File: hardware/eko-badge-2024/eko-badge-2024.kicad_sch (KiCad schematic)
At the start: 51 parts, among them J1 UART, J2 Battery, J3 Lentes, J4 OLED, J7 Battery, P1 USB_C_Plug_USB2.0, Q1 DMG3415U-7, SW1 ON, SW2 LEFT, SW3 UP, SW4 DOWN, SW5 RESET, SW6 BOOT, SW7 RIGTH, U1 ESP32-C6-WROOM-1-N4, U2 AP2112K-3.3, U3 RFM95W-868S2, U4 TPA321

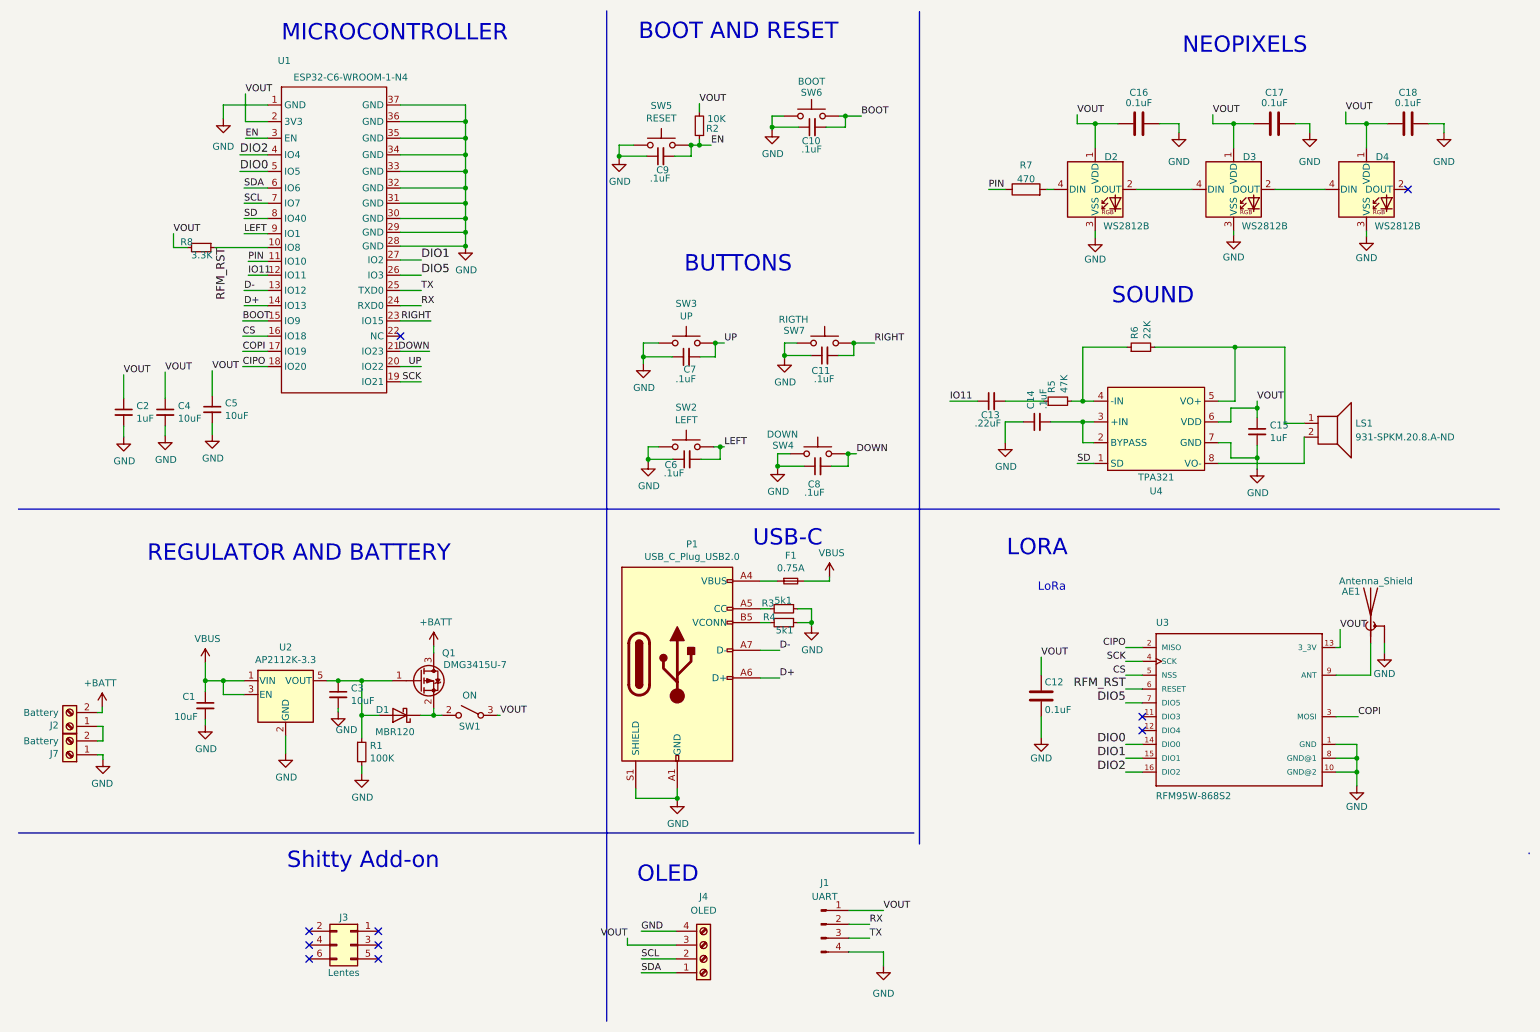
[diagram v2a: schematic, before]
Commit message: feat(Hw):Update_Layer_Distribution
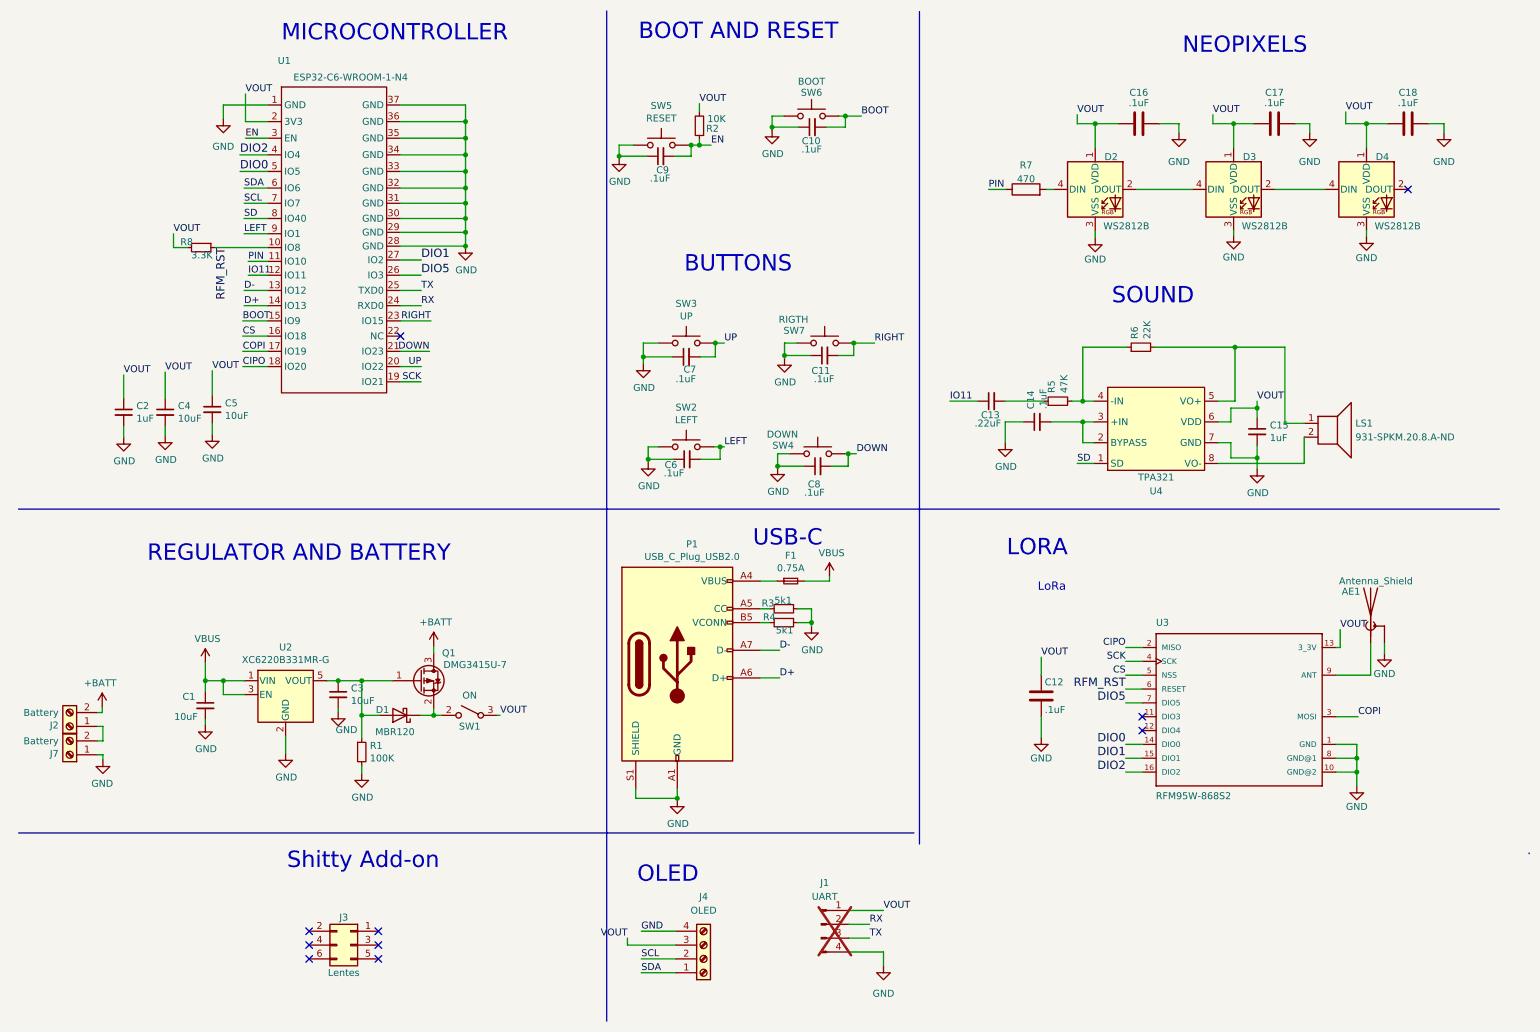
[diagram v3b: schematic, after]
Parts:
- C10, C11, C14, C6, C7, C8, C9: Proveedor (none) -> LCSC; manf# (none) -> 0603F104M500NT
- C12: value 0.1uF -> .1uF; LCSC# C42998 -> C478888; Proveedor (none) -> LCSC
- C13: LCSC# C478888 -> C161213; Proveedor (none) -> LCSC
- C15: Proveedor (none) -> JLCPCB; manf# (none) -> TMK107BJ105KA8T
- C16, C17, C18: value 0.1uF -> .1uF; LCSC# C42998 -> C478888
- J1: now not fitted
- P1: LCSC# C2987386 -> C393939; Proveedor (none) -> LCSC
- SW2, SW3, SW4, SW5, SW6, SW7: Proveedor (none) -> LCSC
- U2: value AP2112K-3.3 -> XC6220B331MR-G; LCSC# C51118 -> C86534; manf# AP2112K3.3TRG -> XC6220B331MR-G
- U3: Proveedor (none) -> Mouser
- U4: LCSC# C329448 -> C2873032; Proveedor (none) -> LCSC
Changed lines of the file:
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@@
 			)
 		)
-		(property "manf#" ""
+		(property "manf#" "0603F104M500NT"
 			(at 198.374 88.138 0)
 			(effects
@@
 			)
 		)
+		(property "Proveedor" "LCSC"
+			(at 198.374 88.138 0)
+			(effects
+				(font
+					(size 1.27 1.27)
+				)
+				(hide yes)
+			)
+		)
 		(pin "1"
 		)
@@
 			)
 		)
-		(property "LCSC#" "C329448"
+		(property "LCSC#" "C2873032"
+			(at 220.218 93.218 0)
+			(effects
+				(font
+					(size 1.27 1.27)
+				)
+				(hide yes)
+			)
+		)
+		(property "Proveedor" "LCSC"
 			(at 220.218 93.218 0)
 			(effects
@@
 			)
 		)
-		(property "manf#" ""
+		(property "manf#" "0603F104M500NT"
 			(at 129.286 39.37 0)
 			(effects
@@
 			)
 		)
+		(property "Proveedor" "LCSC"
+			(at 129.286 39.37 0)
+			(effects
+				(font
+					(size 1.27 1.27)
+				)
+				(hide yes)
+			)
+		)
 		(pin "1"
 		)
@@
 			)
 		)
+		(property "Proveedor" "LCSC"
+			(at 159.385 73.66 0)
+			(effects
+				(font
+					(size 1.27 1.27)
+				)
+				(hide yes)
+			)
+		)
 		(pin "1"
 		)
@@
 			)
 		)
-		(property "Value" "0.1uF"
+		(property "Value" ".1uF"
 			(at 241.935 29.591 90)
 			(effects
@@
 			)
 		)
-		(property "LCSC#" "C42998"
+		(property "LCSC#" "C478888"
 			(at 241.935 33.401 0)
 			(effects
@@
 			)
 		)
+		(property "Proveedor" "LCSC"
+			(at 133.985 73.66 0)
+			(effects
+				(font
+					(size 1.27 1.27)
+				)
+				(hide yes)
+			)
+		)
 		(pin "1"
 		)
@@
 			)
 		)
-		(property "Value" "AP2112K-3.3"
+		(property "Value" "XC6220B331MR-G"
 			(at 60.452 131.8006 0)
 			(effects
@@
 			)
 		)
-		(property "manf#" "AP2112K3.3TRG"
+		(property "manf#" "XC6220B331MR-G "
 			(at 60.452 138.176 0)
 			(effects
@@
 			)
 		)
-		(property "LCSC#" "C51118"
+		(property "LCSC#" "C86534"
 			(at 60.452 138.176 0)
 			(effects
@@
 			)
 		)
-		(property "manf#" ""
+		(property "manf#" "0603F104M500NT"
 			(at 134.112 94.996 0)
 			(effects
@@
 			)
 		)
+		(property "Proveedor" "LCSC"
+			(at 134.112 94.996 0)
+			(effects
+				(font
+					(size 1.27 1.27)
+				)
+				(hide yes)
+			)
+		)
 		(pin "1"
 		)
@@
 			)
 		)
+		(property "Proveedor" "LCSC"
+			(at 133.985 92.71 0)
+			(effects
+				(font
+					(size 1.27 1.27)
+				)
+				(hide yes)
+			)
+		)
 		(pin "1"
 		)
@@
 			)
 		)
-		(property "Value" "0.1uF"
+		(property "Value" ".1uF"
 			(at 217.043 29.591 90)
 			(effects
@@
 			)
 		)
-		(property "LCSC#" "C42998"
+		(property "LCSC#" "C478888"
 			(at 217.043 33.401 0)
 			(effects
@@
 			)
 		)
-		(property "LCSC#" "C478888"
+		(property "LCSC#" "C161213"
+			(at 189.992 84.328 0)
+			(effects
+				(font
+					(size 1.27 1.27)
+				)
+				(hide yes)
+			)
+		)
+		(property "Proveedor" "LCSC"
 			(at 189.992 84.328 0)
 			(effects
@@
 			)
 		)
+		(property "Proveedor" "LCSC"
+			(at 158.115 93.98 0)
+			(effects
+				(font
+					(size 1.27 1.27)
+				)
+				(hide yes)
+			)
+		)
 		(pin "1"
 		)
@@
 			)
 		)
-		(property "Value" "0.1uF"
+		(property "Value" ".1uF"
 			(at 266.446 29.591 90)
 			(effects
@@
 			)
 		)
-		(property "LCSC#" "C42998"
+		(property "LCSC#" "C478888"
 			(at 266.446 33.401 0)
 			(effects
@@
 			)
 		)
+		(property "Proveedor" "LCSC"
+			(at 129.413 37.338 0)
+			(effects
+				(font
+					(size 1.27 1.27)
+				)
+				(hide yes)
+			)
+		)
 		(pin "1"
 		)
@@
 			)
 		)
+		(property "Proveedor" "Mouser"
+			(at 235.458 139.7 0)
+			(effects
+				(font
+					(size 1.27 1.27)
+				)
+				(hide yes)
+			)
+		)
 		(pin "1"
 		)
@@
 			)
 		)
-		(property "manf#" ""
+		(property "manf#" "0603F104M500NT"
 			(at 133.985 76.2 0)
 			(effects
@@
 			)
 		)
+		(property "Proveedor" "LCSC"
+			(at 133.985 76.2 0)
+			(effects
+				(font
+					(size 1.27 1.27)
+				)
+				(hide yes)
+			)
+		)
 		(pin "1"
 		)
@@
 			)
 		)
-		(property "manf#" ""
+		(property "manf#" "0603F104M500NT"
 			(at 158.115 96.266 0)
 			(effects
@@
 			)
 		)
+		(property "Proveedor" "LCSC"
+			(at 158.115 96.266 0)
+			(effects
+				(font
+					(size 1.27 1.27)
+				)
+				(hide yes)
+			)
+		)
 		(pin "1"
 		)
@@
 			)
 		)
-		(property "manf#" ""
+		(property "manf#" "0603F104M500NT"
 			(at 157.099 34.036 0)
 			(effects
@@
 			)
 		)
+		(property "Proveedor" "LCSC"
+			(at 157.099 34.036 0)
+			(effects
+				(font
+					(size 1.27 1.27)
+				)
+				(hide yes)
+			)
+		)
 		(pin "1"
 		)
@@
 			)
 		)
-		(property "Value" "0.1uF"
+		(property "Value" ".1uF"
 			(at 199.771 140.97 0)
 			(effects
@@
 			)
 		)
-		(property "LCSC#" "C42998"
+		(property "LCSC#" "C478888"
+			(at 199.136 138.43 0)
+			(effects
+				(font
+					(size 1.27 1.27)
+				)
+				(hide yes)
+			)
+		)
+		(property "Proveedor" "LCSC"
 			(at 199.136 138.43 0)
 			(effects
@@
 			)
 		)
+		(property "Proveedor" "LCSC"
+			(at 156.972 32.004 0)
+			(effects
+				(font
+					(size 1.27 1.27)
+				)
+				(hide yes)
+			)
+		)
 		(pin "1"
 		)
@@
 			)
 		)
-		(property "manf#" ""
+		(property "manf#" "0603F104M500NT"
 			(at 159.385 75.946 0)
 			(effects
@@
 			)
 		)
+		(property "Proveedor" "LCSC"
+			(at 159.385 75.946 0)
+			(effects
+				(font
+					(size 1.27 1.27)
+				)
+				(hide yes)
+			)
+		)
 		(pin "1"
 		)
@@
 			)
 		)
-		(property "manf#" ""
+		(property "manf#" "TMK107BJ105KA8T"
 			(at 238.76 89.916 0)
 			(effects
@@
 			)
 		)
+		(property "Proveedor" "JLCPCB"
+			(at 238.76 89.916 0)
+			(effects
+				(font
+					(size 1.27 1.27)
+				)
+				(hide yes)
+			)
+		)
 		(pin "1"
 		)
@@
 		(in_bom yes)
 		(on_board yes)
-		(dnp no)
+		(dnp yes)
 		(fields_autoplaced yes)
 		(property "Reference" "J1"
@@
 			)
 		)
-		(property "LCSC#" "C2987386"
+		(property "LCSC#" "C393939"
 			(at 132.334 132.588 0)
 			(effects
@@
 			(at 132.334 132.588 0)
 			(effects
+				(font
+					(size 1.27 1.27)
+				)
+				(hide yes)
+			)
+		)
+		(property "Proveedor" "LCSC"
+			(at 132.334 132.588 0)
+			(effects

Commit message: feat(Hw):Added_Shitty_Add-on
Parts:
- added J5, J6: Add-On, Connector_PinSocket_2.54mm:PinSocket_2x03_P2.54mm_Vertical_SMD, symbol Connector_Generic:Conn_02x03_Odd_Even
- J4: manf# Display Oled Azul y Blanco 128×64 0.96″ I2C SSD1306 -> Display OLED 128×32 0.91 I2C SSD1306 Blanco / Azul
- R6: LCSC# C217281 -> C912502; manf# CR-03JL7---10K -> (none)
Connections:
- net GND: now also J5.2 (Pin_2), J6.2 (Pin_2)
- net VOUT: now also J5.1 (Pin_1), J6.1 (Pin_1)
- no-connect marks 10 -> 18

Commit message: feat(Hw): Update PCB
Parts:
- F1: value 0.75A -> 1A; LCSC# C1972808 -> C2649564; manf# MFU0805FF00750P100 -> MFU0805FF01000P100
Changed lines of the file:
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@@
 			)
 		)
-		(property "Value" "0.75A"
+		(property "Value" "1A"
 			(at 153.162 114.9604 0)
 			(effects
@@
 			)
 		)
-		(property "manf#" "MFU0805FF00750P100 "
+		(property "manf#" "MFU0805FF01000P100"
 			(at 153.162 117.348 0)
 			(effects
@@
 			)
 		)
-		(property "LCSC#" "C1972808"
+		(property "LCSC#" "C2649564"
 			(at 153.162 117.348 0)
 			(effects

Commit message: feat(Hw): Update BOM
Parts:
- U4: Proveedor LCSC -> Mouser; manf# (none) -> TPA321D
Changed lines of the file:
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@@
 			)
 		)
-		(property "Proveedor" "LCSC"
+		(property "Proveedor" "Mouser"
 			(at 220.218 93.218 0)
 			(effects
+				(font
+					(size 1.27 1.27)
+				)
+				(hide yes)
+			)
+		)
+		(property "manf#" "TPA321D"
+			(at 220.218 93.218 0)
+			(effects

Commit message: feat(Hw):Added_details
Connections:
- net GND: now also J3.2 (Pin_2)
- net VOUT: now also J3.1 (Pin_1)
- no-connect marks 18 -> 16
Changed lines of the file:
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@@
 	)
 	(no_connect
-		(at 77.47 181.61)
-	)
-	(no_connect
 		(at 20.066 187.706)
 	)
@@
 	)
 	(no_connect
-		(at 64.77 181.61)
-	)
-	(no_connect
 		(at 64.77 186.69)
 	)
@@
 		)
 	)
+	(wire
+		(pts
+			(xy 61.722 181.61) (xy 64.77 181.61)
+		)
+		(stroke
+			(width 0)
+			(type default)
+		)
+	)
 	(polyline
 		(pts
@@
 	(wire
 		(pts
+			(xy 61.722 181.61) (xy 61.722 181.864)
+		)
+		(stroke
+			(width 0)
+			(type default)
+		)
+	)
+	(wire
+		(pts
 			(xy 161.925 75.946) (xy 164.719 75.946)
 		)
@@
 	(wire
 		(pts
+			(xy 77.47 178.562) (xy 77.47 181.61)
+		)
+		(stroke
+			(width 0)
+			(type default)
+		)
+	)
+	(wire
+		(pts
 			(xy 140.208 94.996) (xy 140.208 92.71)
 		)
@@
 		)
 	)
+	(label "VOUT"
+		(at 77.47 178.562 0)
+		(fields_autoplaced yes)
+		(effects
+			(font
+				(size 1.27 1.27)
+			)
+			(justify left bottom)
+		)
+	)
 	(symbol
 		(lib_id "Connector:Screw_Terminal_01x02")
@@
 					(unit 1)
 				)
+			)
+		)
+	)
+	(symbol
+		(lib_id "power:GND")
+		(at 61.722 181.864 0)
+		(mirror y)
+		(unit 1)
+		(exclude_from_sim no)
+		(in_bom yes)
+		(on_board yes)
+		(dnp no)
+		(property "Reference" "#PWR017"
+			(at 61.722 188.214 0)
+			(effects
+				(font
+					(size 1.27 1.27)
+				)
+				(hide yes)
+			)
+		)
+		(property "Value" "GND"
+			(at 61.595 186.2582 0)
+			(effects
+				(font
+					(size 1.27 1.27)
+				)
+			)
+		)
+		(property "Footprint" ""
+			(at 61.722 181.864 0)
+			(effects
+				(font
+					(size 1.27 1.27)
+				)
+				(hide yes)
+			)
+		)
+		(property "Datasheet" ""
+			(at 61.722 181.864 0)
+			(effects
+				(font
+					(size 1.27 1.27)
+				)
+				(hide yes)
+			)
+		)
+		(property "Description" ""
+			(at 61.722 181.864 0)
+			(effects
+				(font
+					(size 1.27 1.27)
+				)
+				(hide yes)
+			)
+		)
+		(pin "1"
+		)
+		(instances
+			(project "eko-badge-2024"
+				(path "/cbc35911-95a1-4069-b06d-7962aadb895f"
+					(reference "#PWR017")
+					(unit 1)
+				)

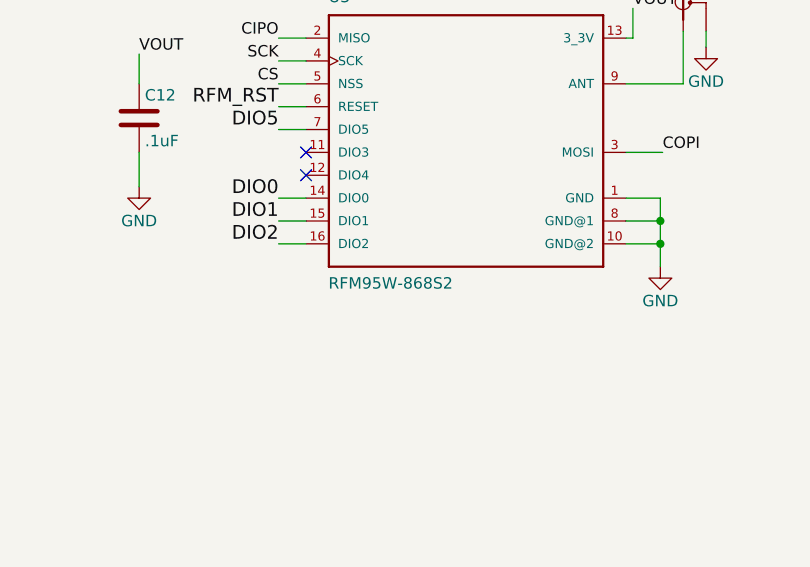
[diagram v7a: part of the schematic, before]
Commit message: fix(hw): update RFM95 module version to 915
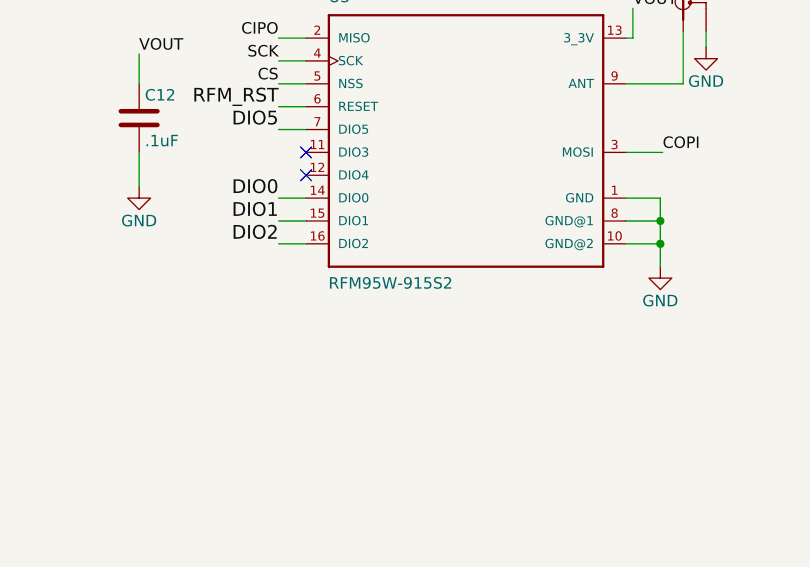
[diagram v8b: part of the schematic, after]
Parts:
- U3: value RFM95W-868S2 -> RFM95W-915S2
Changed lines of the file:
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@@
 			)
 		)
-		(property "Value" "RFM95W-868S2"
+		(property "Value" "RFM95W-915S2"
 			(at 220.1672 157.5308 0)
 			(effects
